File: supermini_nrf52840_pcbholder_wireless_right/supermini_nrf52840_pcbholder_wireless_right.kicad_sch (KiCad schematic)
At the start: 11 parts, among them J1 Conn_01x02, J2 Conn_01x04, J3 Conn_01x07, J4 Conn_01x07, SW1 SW_SPDT, SW2 SW_SPST, U1 nice_nano

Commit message: create left side and tweaks
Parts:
- R1, R2: now not fitted
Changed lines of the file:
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@@
 		(in_bom yes)
 		(on_board yes)
-		(dnp no)
+		(dnp yes)
 		(property "Reference" "R1"
 			(at 85.09 77.4699 90)
@@
 		(in_bom yes)
 		(on_board yes)
-		(dnp no)
+		(dnp yes)
 		(fields_autoplaced yes)
 		(property "Reference" "R2"

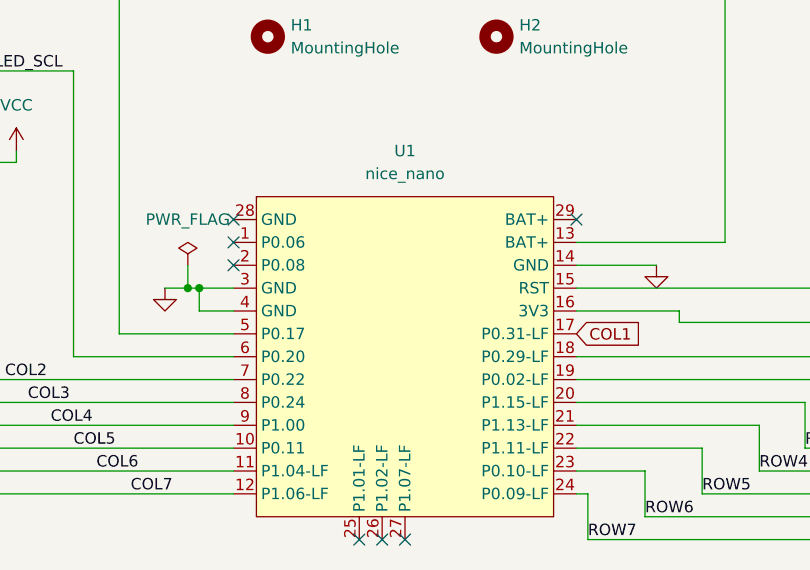
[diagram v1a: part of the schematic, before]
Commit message: remove unused pins from supermini symbol
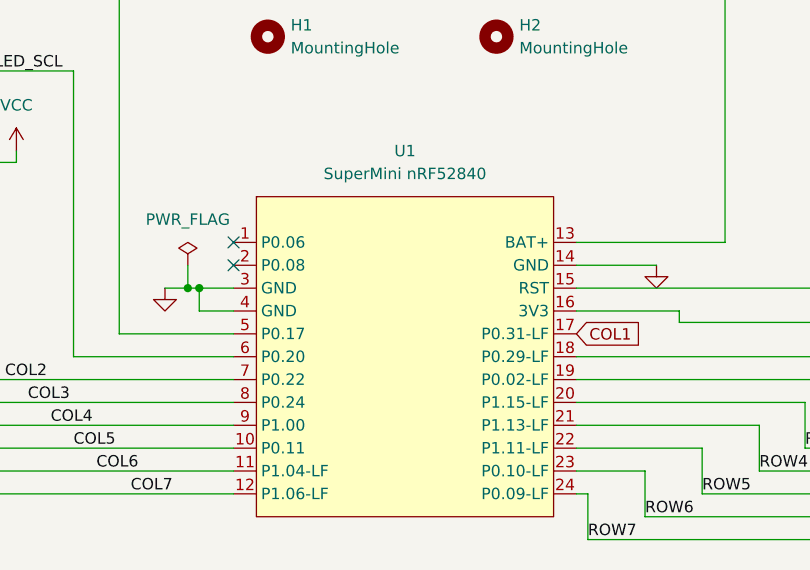
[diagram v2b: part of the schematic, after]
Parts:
- U1: value nice_nano -> SuperMini nRF52840; symbol PCM_marbastlib-promicroish:nice_nano -> Dactyl_SuperMini_Lib:SuperMini_nRF52840_ProMicro
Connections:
- no-connect marks 8 -> 3
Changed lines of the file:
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@@
-	)
-	(no_connect
-		(at 156.21 90.17)
-	)
-	(no_connect
-		(at 134.62 125.73)
 	)
 	(no_connect
@@
 	(no_connect
 		(at 185.42 69.85)
-	)
-	(no_connect
-		(at 137.16 125.73)
-	)
-	(no_connect
-		(at 118.11 90.17)
-	)
-	(no_connect
-		(at 132.08 125.73)
 	)
 	(wire
@@
 	)
 	(symbol
-		(lib_id "PCM_marbastlib-promicroish:nice_nano")
+		(lib_id "Dactyl_SuperMini_Lib:SuperMini_nRF52840_ProMicro")
 		(at 137.16 106.68 0)
 		(unit 1)
@@
 			)
 		)
-		(property "Value" "nice_nano"
+		(property "Value" "SuperMini nRF52840"
 			(at 137.16 85.09 0)
 			(effects
@@
 			)
 		)
-		(property "Datasheet" "https://nicekeyboards.com/docs/nice-nano/pinout-schematic"
+		(property "Datasheet" "https://wiki.icbbuy.com/doku.php?id=developmentboard:nrf52840"
 			(at 138.43 139.7 0)
 			(effects
@@
 			)
 		)
-		(property "Description" "Symbol for an nicekeyboards nice!nano"
+		(property "Description" "Symbol for Supermini nRF52840 with only pro micro compatible pins"
 			(at 137.16 106.68 0)
 			(effects
@@
 		(pin "23"
 		)
-		(pin "25"
-		)
-		(pin "26"
-		)
-		(pin "27"
-		)
-		(pin "28"
-		)
 		(pin "24"
 		)
@@
 		(pin "7"
 		)
-		(pin "29"
-		)
 		(pin "17"
